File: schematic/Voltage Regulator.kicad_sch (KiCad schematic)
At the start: 3 parts, among them U3 LD1117S33TR

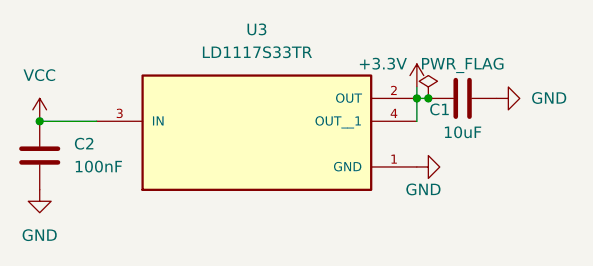
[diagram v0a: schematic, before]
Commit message: Changed to Kicad Version 8
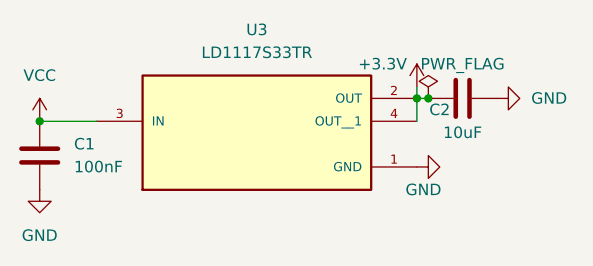
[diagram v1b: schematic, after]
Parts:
- renumbered C2 to C1, C1 to C2
